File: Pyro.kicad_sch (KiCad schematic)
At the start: 4 parts, among them Q1 IRFML8244TRPBF

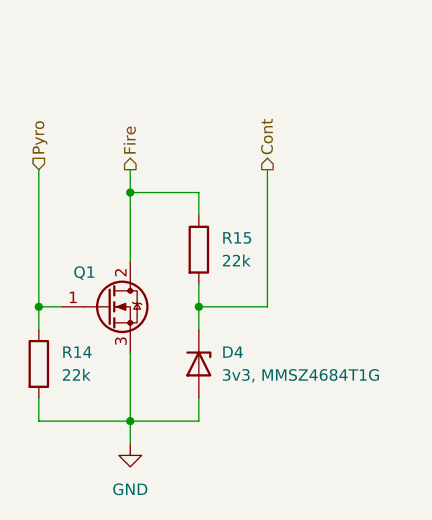
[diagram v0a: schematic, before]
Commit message: Reworked pyro channel to use clamping diodes
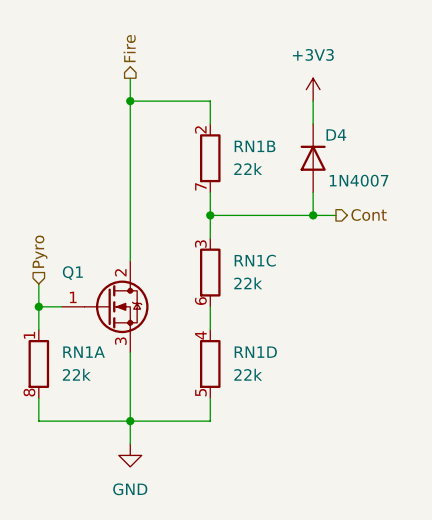
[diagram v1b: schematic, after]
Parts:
- removed D4: 3v3, MMSZ4684T1G, Diode_SMD:D_SOD-123, symbol Device:D_Zener
- removed R14, R15: 22k, symbol Device:R
- added D4: 1N4007, Diode_SMD:D_SOD-123, symbol Diode:1N914
- added RN1: 22k, Resistor_SMD:R_Array_Convex_4x1206, symbol Device:R_Pack04_Split
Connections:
- net Cont: now also D4.2 (A), RN1.3 (R3.1), RN1.7 (R2.2)
- net Fire: now also RN1.2 (R2.1)
- net GND: now also RN1.5 (R4.2), RN1.8 (R1.2)
- net Pyro: now also RN1.1 (R1.1)
- new net: RN1.4 (R4.1), RN1.6 (R3.2)
- new net +3V3: D4.1 (K)

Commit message: Connected the sensors, flash chip, Need to connect the radio and GPS
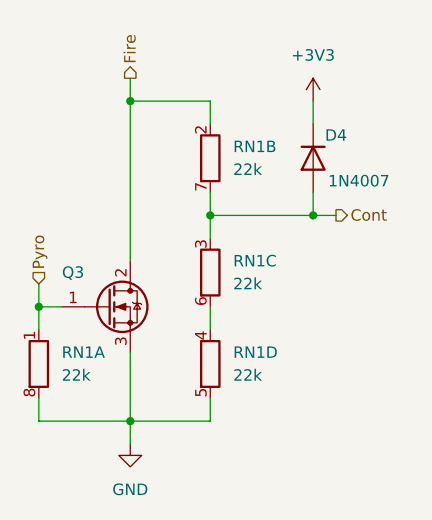
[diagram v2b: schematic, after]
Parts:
- renumbered Q1 to Q3
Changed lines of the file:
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@@
   (symbol (lib_id "power:GND") (at 100.33 82.55 0) (unit 1)
     (in_bom yes) (on_board yes) (fields_autoplaced)
-    (property "Reference" "#PWR058" (id 0) (at 100.33 88.9 0)
+    (property "Reference" "#PWR065" (id 0) (at 100.33 88.9 0)
       (effects (font (size 1.27 1.27)) hide)
     )
@@
   (symbol (lib_id "Device:Q_NMOS_GDS") (at 97.79 67.31 0) (unit 1)
     (in_bom yes) (on_board yes)
-    (property "Reference" "Q1" (id 0) (at 93.98 63.5 0))
+    (property "Reference" "Q3" (id 0) (at 93.98 63.5 0))
     (property "Value" "    IRFML8244TRPBF" (id 1) (at 85.09 69.85 0)
       (effects (font (size 1.27 1.27)) hide)
@@
   (symbol (lib_id "power:+3V3") (at 120.65 44.45 0) (unit 1)
     (in_bom yes) (on_board yes) (fields_autoplaced)
-    (property "Reference" "#PWR070" (id 0) (at 120.65 48.26 0)
+    (property "Reference" "#PWR066" (id 0) (at 120.65 48.26 0)
       (effects (font (size 1.27 1.27)) hide)
     )

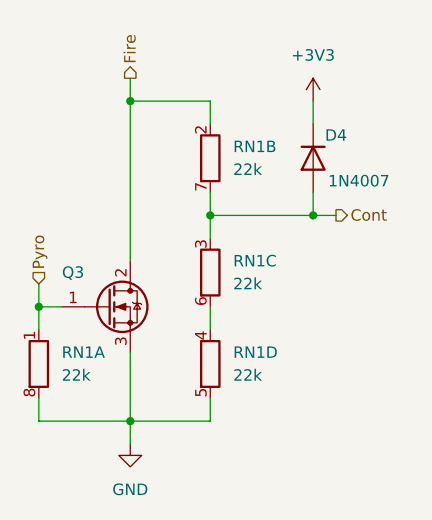
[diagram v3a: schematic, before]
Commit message: Added polyfuse
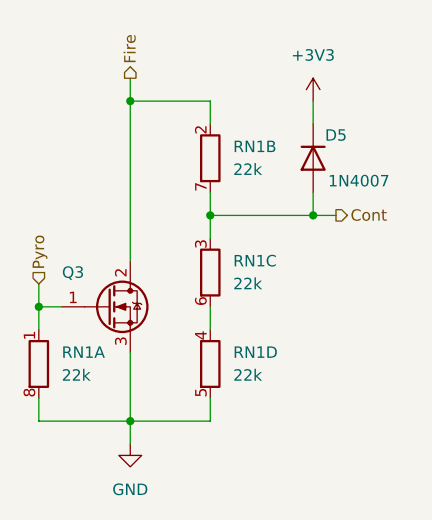
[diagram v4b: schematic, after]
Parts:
- RN1: footprint Resistor_SMD:R_Array_Convex_4x1206 -> Resistor_SMD:R_Array_Convex_4x0603
- renumbered D4 to D5
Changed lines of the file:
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@@
       (effects (font (size 1.27 1.27)) (justify right))
     )
-    (property "Footprint" "Resistor_SMD:R_Array_Convex_4x1206" (id 2) (at 111.252 50.8 90)
+    (property "Footprint" "Resistor_SMD:R_Array_Convex_4x0603" (id 2) (at 111.252 50.8 90)
       (effects (font (size 1.27 1.27)) hide)
     )
@@
       (effects (font (size 1.27 1.27)) (justify right))
     )
-    (property "Footprint" "Resistor_SMD:R_Array_Convex_4x1206" (id 2) (at 111.252 63.5 90)
+    (property "Footprint" "Resistor_SMD:R_Array_Convex_4x0603" (id 2) (at 111.252 63.5 90)
       (effects (font (size 1.27 1.27)) hide)
     )
@@
   (symbol (lib_id "power:GND") (at 100.33 82.55 0) (unit 1)
     (in_bom yes) (on_board yes) (fields_autoplaced)
-    (property "Reference" "#PWR065" (id 0) (at 100.33 88.9 0)
+    (property "Reference" "#PWR059" (id 0) (at 100.33 88.9 0)
       (effects (font (size 1.27 1.27)) hide)
     )
@@
   (symbol (lib_id "Diode:1N914") (at 120.65 50.8 90) (mirror x) (unit 1)
     (in_bom yes) (on_board yes)
-    (property "Reference" "D4" (id 0) (at 123.19 48.26 90))
+    (property "Reference" "D5" (id 0) (at 123.19 48.26 90))
     (property "Value" "1N4007" (id 1) (at 125.73 53.34 90))
     (property "Footprint" "Diode_SMD:D_SOD-123" (id 2) (at 125.095 50.8 0)
@@
       (effects (font (size 1.27 1.27)) (justify right))
     )
-    (property "Footprint" "Resistor_SMD:R_Array_Convex_4x1206" (id 2) (at 92.202 73.66 90)
+    (property "Footprint" "Resistor_SMD:R_Array_Convex_4x0603" (id 2) (at 92.202 73.66 90)
       (effects (font (size 1.27 1.27)) hide)
     )
@@
       (effects (font (size 1.27 1.27)) (justify right))
     )
-    (property "Footprint" "Resistor_SMD:R_Array_Convex_4x1206" (id 2) (at 111.252 73.66 90)
+    (property "Footprint" "Resistor_SMD:R_Array_Convex_4x0603" (id 2) (at 111.252 73.66 90)
       (effects (font (size 1.27 1.27)) hide)
     )
@@
   (symbol (lib_id "power:+3V3") (at 120.65 44.45 0) (unit 1)
     (in_bom yes) (on_board yes) (fields_autoplaced)
-    (property "Reference" "#PWR066" (id 0) (at 120.65 48.26 0)
+    (property "Reference" "#PWR060" (id 0) (at 120.65 48.26 0)
       (effects (font (size 1.27 1.27)) hide)
     )

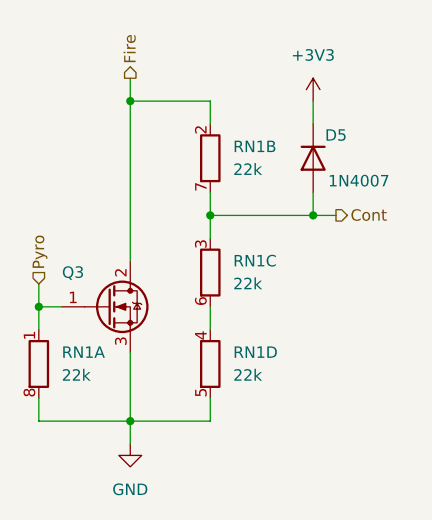
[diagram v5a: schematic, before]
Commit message: Geographical reannotated
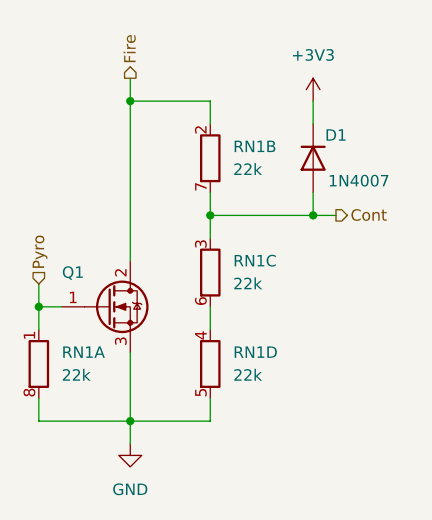
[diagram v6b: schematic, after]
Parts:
- renumbered D5 to D1, Q3 to Q1
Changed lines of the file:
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@@
   (symbol (lib_id "Device:Q_NMOS_GDS") (at 97.79 67.31 0) (unit 1)
     (in_bom yes) (on_board yes)
-    (property "Reference" "Q3" (id 0) (at 93.98 63.5 0))
+    (property "Reference" "Q1" (id 0) (at 93.98 63.5 0))
     (property "Value" "    IRFML8244TRPBF" (id 1) (at 85.09 69.85 0)
       (effects (font (size 1.27 1.27)) hide)
@@
   (symbol (lib_id "Diode:1N914") (at 120.65 50.8 90) (mirror x) (unit 1)
     (in_bom yes) (on_board yes)
-    (property "Reference" "D5" (id 0) (at 123.19 48.26 90))
+    (property "Reference" "D1" (id 0) (at 123.19 48.26 90))
     (property "Value" "1N4007" (id 1) (at 125.73 53.34 90))
     (property "Footprint" "Diode_SMD:D_SOD-123" (id 2) (at 125.095 50.8 0)

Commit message: Final refinements before issue to JLC
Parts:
- renumbered D1 to D5, Q1 to Q3
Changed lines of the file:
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@@
   (symbol (lib_id "power:GND") (at 100.33 82.55 0) (unit 1)
     (in_bom yes) (on_board yes) (fields_autoplaced)
-    (property "Reference" "#PWR069" (id 0) (at 100.33 88.9 0)
+    (property "Reference" "#PWR071" (id 0) (at 100.33 88.9 0)
       (effects (font (size 1.27 1.27)) hide)
     )
@@
   (symbol (lib_id "Device:Q_NMOS_GDS") (at 97.79 67.31 0) (unit 1)
     (in_bom yes) (on_board yes)
-    (property "Reference" "Q1" (id 0) (at 93.98 63.5 0))
+    (property "Reference" "Q3" (id 0) (at 93.98 63.5 0))
     (property "Value" "    IRFML8244TRPBF" (id 1) (at 85.09 69.85 0)
       (effects (font (size 1.27 1.27)) hide)
@@
   (symbol (lib_id "Diode:1N914") (at 120.65 50.8 90) (mirror x) (unit 1)
     (in_bom yes) (on_board yes)
-    (property "Reference" "D1" (id 0) (at 123.19 48.26 90))
+    (property "Reference" "D5" (id 0) (at 123.19 48.26 90))
     (property "Value" "1N4007" (id 1) (at 125.73 53.34 90))
     (property "Footprint" "Diode_SMD:D_SOD-123" (id 2) (at 125.095 50.8 0)
@@
   (symbol (lib_id "power:+3V3") (at 120.65 44.45 0) (unit 1)
     (in_bom yes) (on_board yes) (fields_autoplaced)
-    (property "Reference" "#PWR070" (id 0) (at 120.65 48.26 0)
+    (property "Reference" "#PWR072" (id 0) (at 120.65 48.26 0)
       (effects (font (size 1.27 1.27)) hide)
     )
